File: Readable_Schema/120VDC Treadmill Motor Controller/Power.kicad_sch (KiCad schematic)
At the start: 21 parts, among them J1 TB005-762-03BE, J6 TB0011-350-03BE, J7 OSTT7020150, K1 T9GV1L14-24, Q5 IPP60R060P7XKSA1, U5 TPSI3050QDWZRQ1

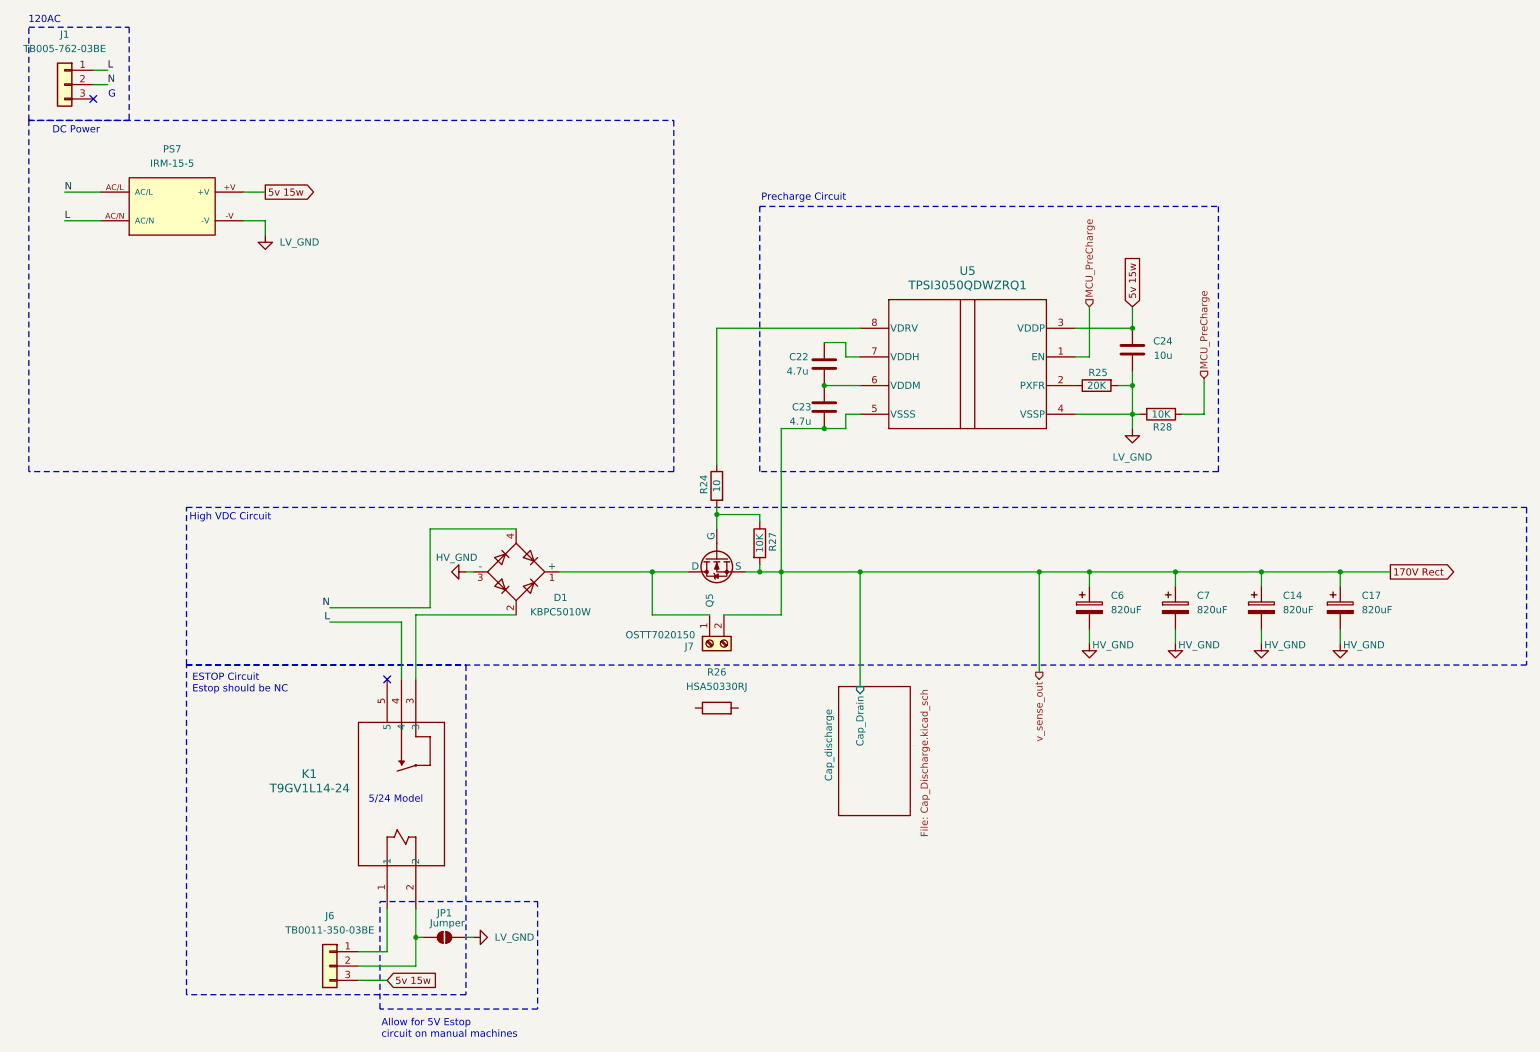
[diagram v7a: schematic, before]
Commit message: -Think we're finished with the schematic (finally) --Upped the LED resistors and added a few more supporting caps for the 3.3v iso supply in the feedback schema
-Started placing footprints
--Now that we're using how air instead of oven I'm not going to try and keep all SMD components on the same side anymore
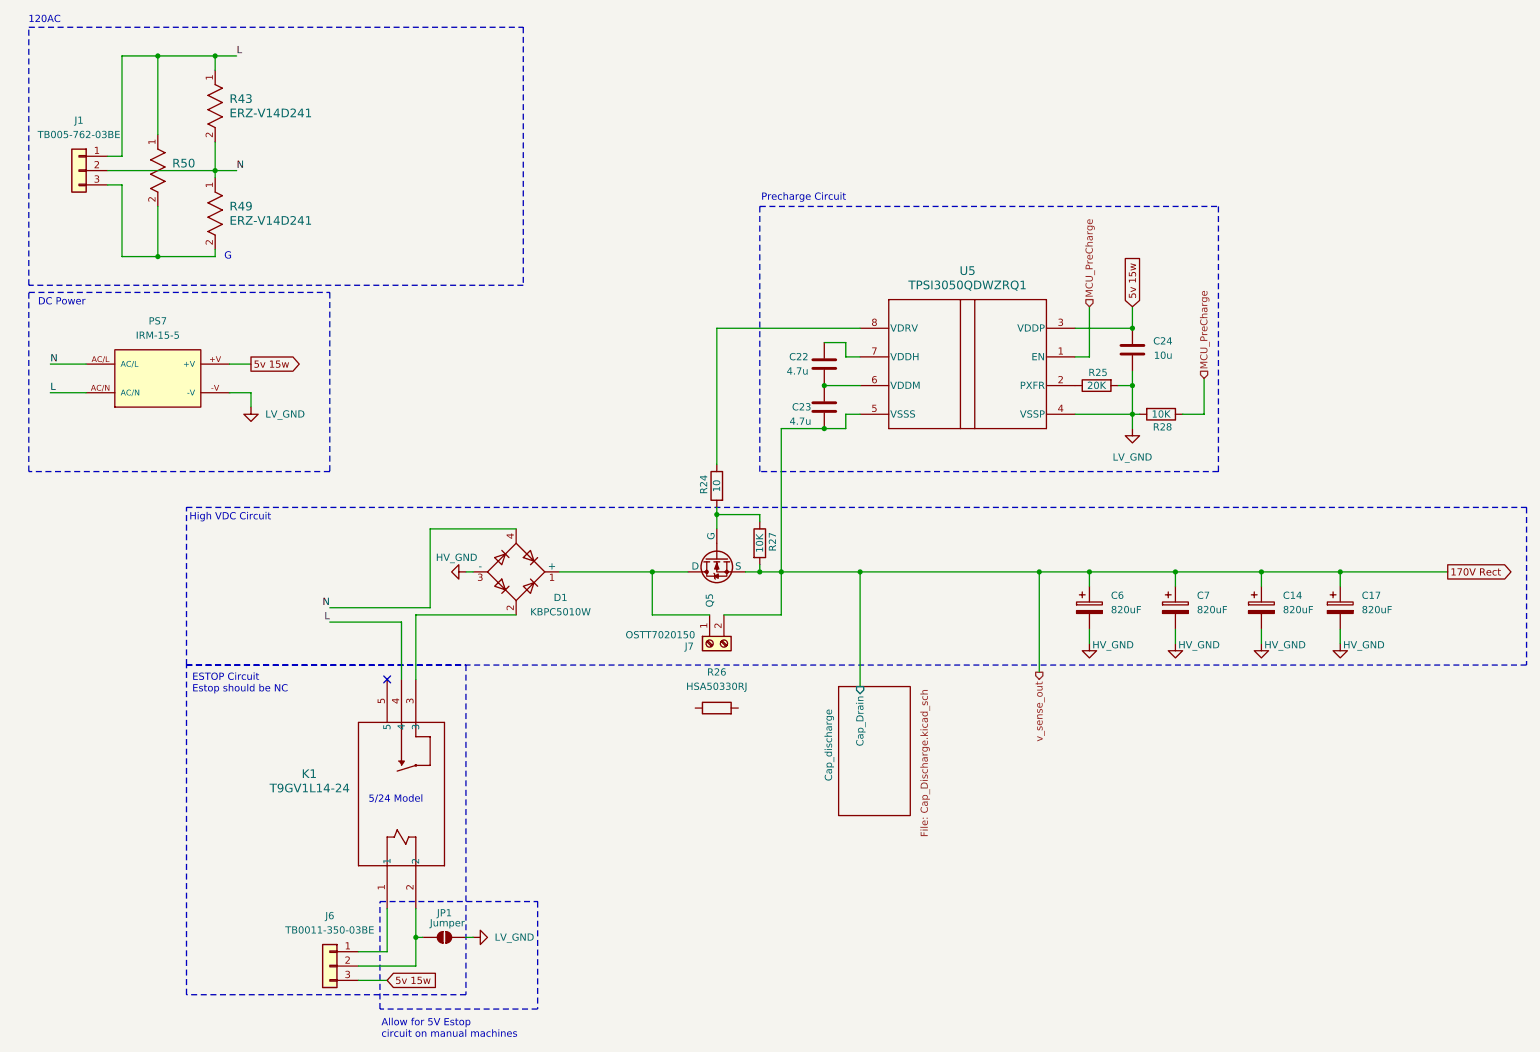
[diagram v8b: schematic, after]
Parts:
- added R43, R49, R50: ERZ-V14D241, Treadmill_Feet:RES_ERZ-V14D241_PAN, symbol Treadmill_Comp:ERZ-V14D241
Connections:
- net L: now also R43.1, R50.1
- net N: now also R43.2, R49.1
- net at J1.3 (Pin_3): now also R49.2, R50.2
- no-connect marks 2 -> 1
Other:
- moved on the sheet: J1, PS7
